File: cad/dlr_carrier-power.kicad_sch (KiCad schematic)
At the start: 17 parts, among them U1 AP2112K-3.3, U2 LP5907MFX-3.8, U9 LMR33630ADDA

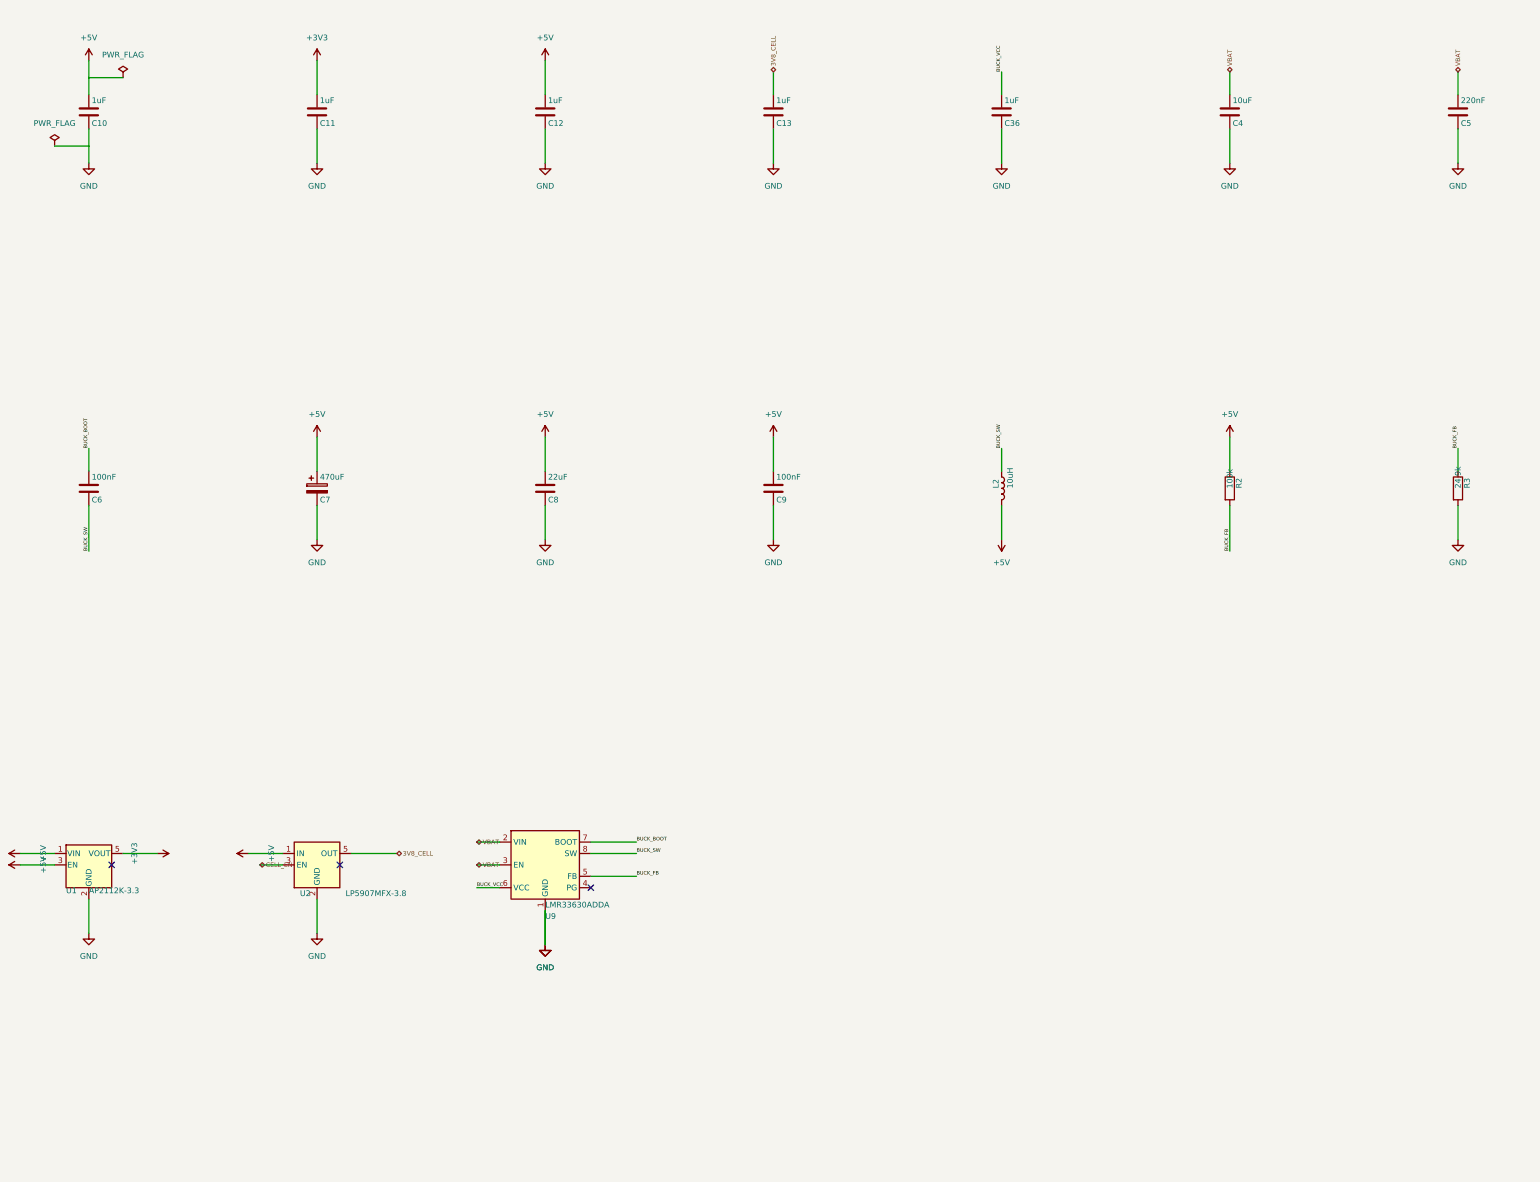
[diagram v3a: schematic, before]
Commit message: 🩺 refactor(schematic): cross-sheet nets via global labels, no sheet pins
Three attempts at making the hierarchical sheet-pin mechanism pass KiCad 9 failed
(project name, instance paths, label type), so the mechanism goes. Cross-sheet nets
now connect by name through global labels on the child sheets; the root carries
sheet symbols only — no pins, no stub wires, no labels.

That removes the whole hier_label_mismatch / label_dangling class rather than
chasing it, and it matches the connectivity style the generate-schematic skill
already prescribes for this project ("all inter-block connections use net labels").

kicad-sch-api's add_global_label still does not serialize, so the labels are emitted
as hierarchical and rewritten in the saved sheet.

Co-Authored-By: Claude Opus 5 <noreply@anthropic.com>
Claude-Session: https://claude.ai/code/session_011xr7VCL7rkJj2WE2uQF7sF
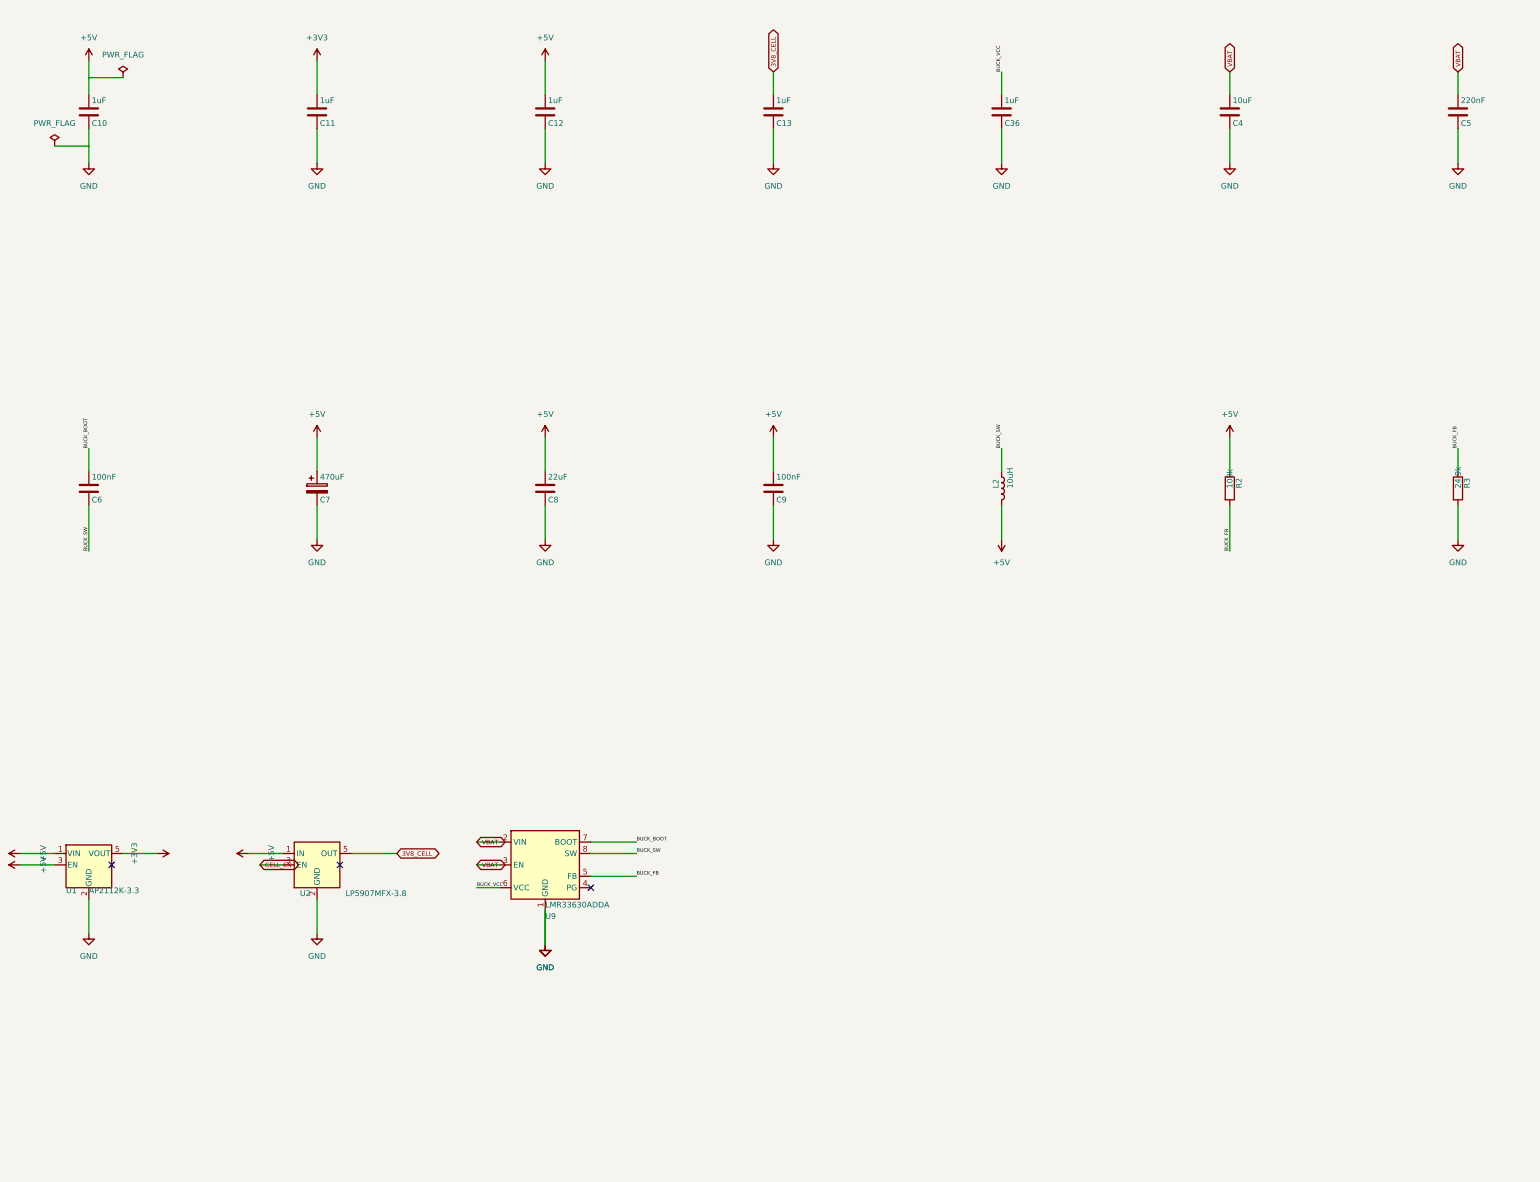
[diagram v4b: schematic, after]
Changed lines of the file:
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@@
 		(instances
 			(project "POWER RAILS"
-				(path "/b92f7d05-346d-4153-84be-6036ac927b56"
+				(path "/739cf134-3086-4ab2-aba3-5ec48d60810b"
 					(reference "C10")
 					(unit 1)
@@
 		(instances
 			(project "POWER RAILS"
-				(path "/b92f7d05-346d-4153-84be-6036ac927b56"
+				(path "/739cf134-3086-4ab2-aba3-5ec48d60810b"
 					(reference "C11")
 					(unit 1)
@@
 		(instances
 			(project "POWER RAILS"
-				(path "/b92f7d05-346d-4153-84be-6036ac927b56"
+				(path "/739cf134-3086-4ab2-aba3-5ec48d60810b"
 					(reference "C12")
 					(unit 1)
@@
 		(instances
 			(project "POWER RAILS"
-				(path "/b92f7d05-346d-4153-84be-6036ac927b56"
+				(path "/739cf134-3086-4ab2-aba3-5ec48d60810b"
 					(reference "C13")
 					(unit 1)
@@
 		(instances
 			(project "POWER RAILS"
-				(path "/b92f7d05-346d-4153-84be-6036ac927b56"
+				(path "/739cf134-3086-4ab2-aba3-5ec48d60810b"
 					(reference "C36")
 					(unit 1)
@@
 		(instances
 			(project "POWER RAILS"
-				(path "/b92f7d05-346d-4153-84be-6036ac927b56"
+				(path "/739cf134-3086-4ab2-aba3-5ec48d60810b"
 					(reference "C4")
 					(unit 1)
@@
 		(instances
 			(project "POWER RAILS"
-				(path "/b92f7d05-346d-4153-84be-6036ac927b56"
+				(path "/739cf134-3086-4ab2-aba3-5ec48d60810b"
 					(reference "C5")
 					(unit 1)
@@
 		(instances
 			(project "POWER RAILS"
-				(path "/b92f7d05-346d-4153-84be-6036ac927b56"
+				(path "/739cf134-3086-4ab2-aba3-5ec48d60810b"
 					(reference "C6")
 					(unit 1)
@@
 		(instances
 			(project "POWER RAILS"
-				(path "/b92f7d05-346d-4153-84be-6036ac927b56"
+				(path "/739cf134-3086-4ab2-aba3-5ec48d60810b"
 					(reference "C7")
 					(unit 1)
@@
 		(instances
 			(project "POWER RAILS"
-				(path "/b92f7d05-346d-4153-84be-6036ac927b56"
+				(path "/739cf134-3086-4ab2-aba3-5ec48d60810b"
 					(reference "C8")
 					(unit 1)
@@
 		(instances
 			(project "POWER RAILS"
-				(path "/b92f7d05-346d-4153-84be-6036ac927b56"
+				(path "/739cf134-3086-4ab2-aba3-5ec48d60810b"
 					(reference "C9")
 					(unit 1)
@@
 		(instances
 			(project "POWER RAILS"
-				(path "/b92f7d05-346d-4153-84be-6036ac927b56"
+				(path "/739cf134-3086-4ab2-aba3-5ec48d60810b"
 					(reference "L2")
 					(unit 1)
@@
 		(instances
 			(project "POWER RAILS"
-				(path "/b92f7d05-346d-4153-84be-6036ac927b56"
+				(path "/739cf134-3086-4ab2-aba3-5ec48d60810b"
 					(reference "R2")
 					(unit 1)
@@
 		(instances
 			(project "POWER RAILS"
-				(path "/b92f7d05-346d-4153-84be-6036ac927b56"
+				(path "/739cf134-3086-4ab2-aba3-5ec48d60810b"
 					(reference "R3")
 					(unit 1)
@@
 		(instances
 			(project "POWER RAILS"
-				(path "/b92f7d05-346d-4153-84be-6036ac927b56"
+				(path "/739cf134-3086-4ab2-aba3-5ec48d60810b"
 					(reference "U1")
 					(unit 1)
@@
 		(instances
 			(project "POWER RAILS"
-				(path "/b92f7d05-346d-4153-84be-6036ac927b56"
+				(path "/739cf134-3086-4ab2-aba3-5ec48d60810b"
 					(reference "U2")
 					(unit 1)
@@
 		(instances
 			(project "POWER RAILS"
-				(path "/b92f7d05-346d-4153-84be-6036ac927b56"
+				(path "/739cf134-3086-4ab2-aba3-5ec48d60810b"
 					(reference "U9")
 					(unit 1)
@@
 		(instances
 			(project "POWER RAILS"
-				(path "/b92f7d05-346d-4153-84be-6036ac927b56"
+				(path "/739cf134-3086-4ab2-aba3-5ec48d60810b"
 					(reference "#PWR001")
 					(unit 1)
@@
 		(instances
 			(project "POWER RAILS"
-				(path "/b92f7d05-346d-4153-84be-6036ac927b56"
+				(path "/739cf134-3086-4ab2-aba3-5ec48d60810b"
 					(reference "#PWR002")
 					(unit 1)
@@
 		(instances
 			(project "POWER RAILS"
-				(path "/b92f7d05-346d-4153-84be-6036ac927b56"
+				(path "/739cf134-3086-4ab2-aba3-5ec48d60810b"
 					(reference "#FLG001")
 					(unit 1)
@@
 		(instances
 			(project "POWER RAILS"
-				(path "/b92f7d05-346d-4153-84be-6036ac927b56"
+				(path "/739cf134-3086-4ab2-aba3-5ec48d60810b"
 					(reference "#PWR003")
 					(unit 1)
@@
 		(instances
 			(project "POWER RAILS"
-				(path "/b92f7d05-346d-4153-84be-6036ac927b56"
+				(path "/739cf134-3086-4ab2-aba3-5ec48d60810b"
 					(reference "#PWR004")
 					(unit 1)
@@
 		(instances
 			(project "POWER RAILS"
-				(path "/b92f7d05-346d-4153-84be-6036ac927b56"
+				(path "/739cf134-3086-4ab2-aba3-5ec48d60810b"
 					(reference "#PWR005")
 					(unit 1)
@@
 		(instances
 			(project "POWER RAILS"
-				(path "/b92f7d05-346d-4153-84be-6036ac927b56"
+				(path "/739cf134-3086-4ab2-aba3-5ec48d60810b"
 					(reference "#PWR006")
 					(unit 1)
@@
 		(instances
 			(project "POWER RAILS"
-				(path "/b92f7d05-346d-4153-84be-6036ac927b56"
+				(path "/739cf134-3086-4ab2-aba3-5ec48d60810b"
 					(reference "#PWR007")
 					(unit 1)
@@
 		(instances
 			(project "POWER RAILS"
-				(path "/b92f7d05-346d-4153-84be-6036ac927b56"
+				(path "/739cf134-3086-4ab2-aba3-5ec48d60810b"
 					(reference "#PWR008")
 					(unit 1)
@@
 		(instances
 			(project "POWER RAILS"
-				(path "/b92f7d05-346d-4153-84be-6036ac927b56"
+				(path "/739cf134-3086-4ab2-aba3-5ec48d60810b"
 					(reference "#PWR009")
 					(unit 1)
@@
 		(instances
 			(project "POWER RAILS"
-				(path "/b92f7d05-346d-4153-84be-6036ac927b56"
+				(path "/739cf134-3086-4ab2-aba3-5ec48d60810b"
 					(reference "#PWR010")
 					(unit 1)
@@
 		(instances
 			(project "POWER RAILS"
-				(path "/b92f7d05-346d-4153-84be-6036ac927b56"
+				(path "/739cf134-3086-4ab2-aba3-5ec48d60810b"
 					(reference "#PWR011")
 					(unit 1)
@@
 		(instances
 			(project "POWER RAILS"
-				(path "/b92f7d05-346d-4153-84be-6036ac927b56"
+				(path "/739cf134-3086-4ab2-aba3-5ec48d60810b"
 					(reference "#PWR012")
 					(unit 1)
@@
 		(instances
 			(project "POWER RAILS"
-				(path "/b92f7d05-346d-4153-84be-6036ac927b56"
+				(path "/739cf134-3086-4ab2-aba3-5ec48d60810b"
 					(reference "#FLG002")
 					(unit 1)
@@
 		(instances
 			(project "POWER RAILS"
-				(path "/b92f7d05-346d-4153-84be-6036ac927b56"
+				(path "/739cf134-3086-4ab2-aba3-5ec48d60810b"
 					(reference "#PWR013")
 					(unit 1)
@@
 		(instances
 			(project "POWER RAILS"
-				(path "/b92f7d05-346d-4153-84be-6036ac927b56"
+				(path "/739cf134-3086-4ab2-aba3-5ec48d60810b"
 					(reference "#PWR014")
 					(unit 1)
@@
 		(instances
 			(project "POWER RAILS"
-				(path "/b92f7d05-346d-4153-84be-6036ac927b56"
+				(path "/739cf134-3086-4ab2-aba3-5ec48d60810b"
 					(reference "#PWR015")
 					(unit 1)
@@
 		(instances
 			(project "POWER RAILS"
-				(path "/b92f7d05-346d-4153-84be-6036ac927b56"
+				(path "/739cf134-3086-4ab2-aba3-5ec48d60810b"
 					(reference "#PWR016")
 					(unit 1)
@@
 		(instances
 			(project "POWER RAILS"
-				(path "/b92f7d05-346d-4153-84be-6036ac927b56"
+				(path "/739cf134-3086-4ab2-aba3-5ec48d60810b"
 					(reference "#PWR017")
 					(unit 1)
@@
 		(instances
 			(project "POWER RAILS"
-				(path "/b92f7d05-346d-4153-84be-6036ac927b56"
+				(path "/739cf134-3086-4ab2-aba3-5ec48d60810b"
 					(reference "#PWR018")
 					(unit 1)
@@
 		(instances
 			(project "POWER RAILS"
-				(path "/b92f7d05-346d-4153-84be-6036ac927b56"
+				(path "/739cf134-3086-4ab2-aba3-5ec48d60810b"
 					(reference "#PWR019")
 					(unit 1)
@@
 		(instances
 			(project "POWER RAILS"
-				(path "/b92f7d05-346d-4153-84be-6036ac927b56"
+				(path "/739cf134-3086-4ab2-aba3-5ec48d60810b"
 					(reference "#PWR020")
 					(unit 1)
@@
 		(instances
 			(project "POWER RAILS"
-				(path "/b92f7d05-346d-4153-84be-6036ac927b56"
+				(path "/739cf134-3086-4ab2-aba3-5ec48d60810b"
 					(reference "#PWR021")
 					(unit 1)
@@
 		(instances
 			(project "POWER RAILS"
-				(path "/b92f7d05-346d-4153-84be-6036ac927b56"
+				(path "/739cf134-3086-4ab2-aba3-5ec48d60810b"
 					(reference "#PWR022")
 					(unit 1)
@@
 		(instances
 			(project "POWER RAILS"
-				(path "/b92f7d05-346d-4153-84be-6036ac927b56"
+				(path "/739cf134-3086-4ab2-aba3-5ec48d60810b"
 					(reference "#PWR023")
 					(unit 1)
@@
 		(instances
 			(project "POWER RAILS"
-				(path "/b92f7d05-346d-4153-84be-6036ac927b56"
+				(path "/739cf134-3086-4ab2-aba3-5ec48d60810b"
 					(reference "#PWR024")
 					(unit 1)
@@
 		(instances
 			(project "POWER RAILS"
-				(path "/b92f7d05-346d-4153-84be-6036ac927b56"
+				(path "/739cf134-3086-4ab2-aba3-5ec48d60810b"
 					(reference "#PWR025")
 					(unit 1)
@@
 		(instances
 			(project "POWER RAILS"
-				(path "/b92f7d05-346d-4153-84be-6036ac927b56"
+				(path "/739cf134-3086-4ab2-aba3-5ec48d60810b"
 					(reference "#PWR026")
 					(unit 1)
@@
 		(instances
 			(project "POWER RAILS"
-				(path "/b92f7d05-346d-4153-84be-6036ac927b56"
+				(path "/739cf134-3086-4ab2-aba3-5ec48d60810b"
 					(reference "#PWR027")
 					(unit 1)
@@
 		)
 	)
-	(hierarchical_label "3V8_CELL"
+	(global_label "3V8_CELL"
 		(shape bidirectional)
 		(at 215.9 71.12 90)
@@
 		)
 	)
-	(hierarchical_label "3V8_CELL"
+	(global_label "3V8_CELL"
 		(shape bidirectional)
 		(at 132.08 245.11 0)
@@
 		)
 	)
-	(hierarchical_label "CELL_EN"
+	(global_label "CELL_EN"
 		(shape bidirectional)
 		(at 101.6 247.65 180)
@@
 		)
 	)
-	(hierarchical_label "VBAT"
+	(global_label "VBAT"
 		(shape bidirectional)
 		(at 317.5 71.12 90)
@@
 		)
 	)
-	(hierarchical_label "VBAT"
+	(global_label "VBAT"
 		(shape bidirectional)
 		(at 368.3 71.12 90)
@@
 		)
 	)
-	(hierarchical_label "VBAT"
+	(global_label "VBAT"
 		(shape bidirectional)
 		(at 149.86 242.57 180)
@@
 		)
 	)
-	(hierarchical_label "VBAT"
+	(global_label "VBAT"
 		(shape bidirectional)
 		(at 149.86 247.65 180)
@@
 	)
 	(sheet_instances
-		(path "/c5c169f4-6c30-478e-8391-6862f9d11774"
+		(path "/37aa6935-320b-4577-b92b-8faeebcd5e37"
 			(page "3")
 		)
